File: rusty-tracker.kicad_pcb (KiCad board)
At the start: 4 copper layers, 50 x 85 mm, 172 parts, among them J1 SIM8051-6-0-14-01-X, J2 USB_C_Receptacle_USB2.0, J3 NFC, J4 tag-connect-swd, J5 Battery Connector, Q1 BC846, Q2 BC846, SW1 SW_Push, T1 Tab, T2 Tab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

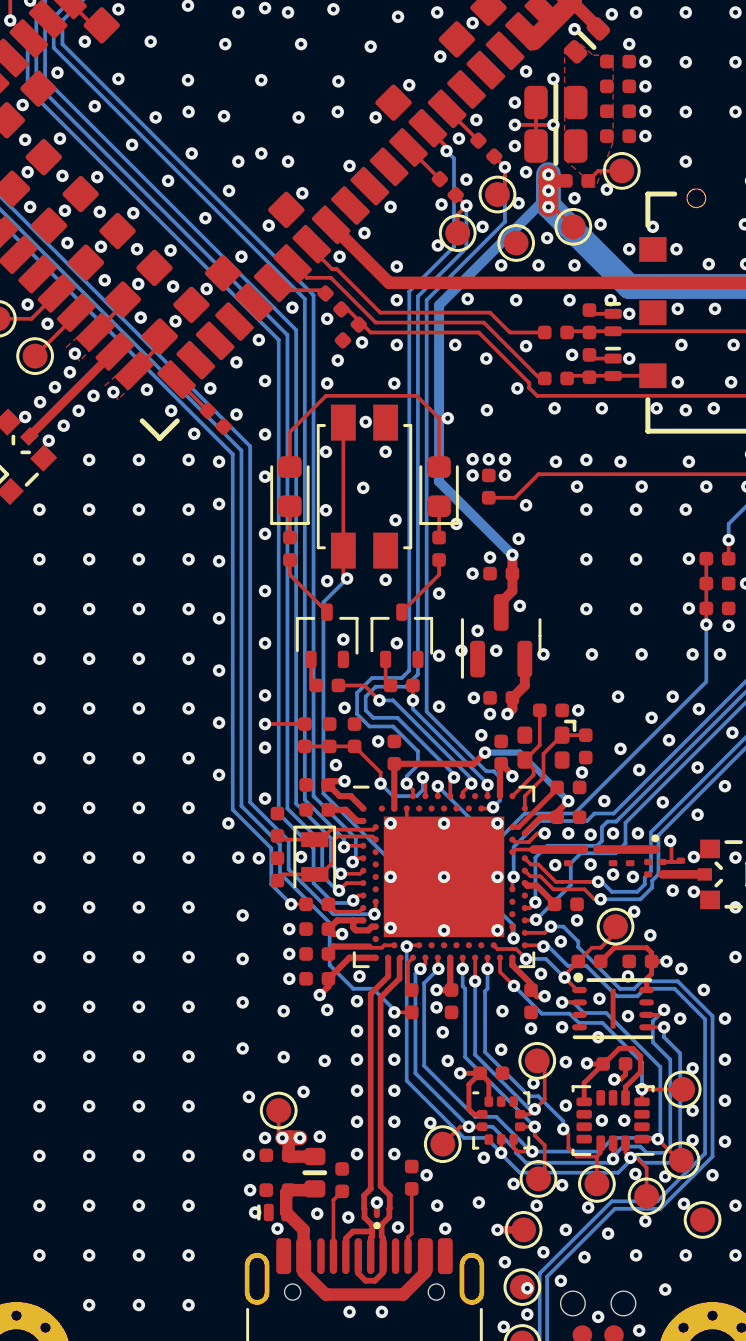
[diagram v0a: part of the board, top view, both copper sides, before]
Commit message: Add support for VBAT -> VDDH, and DCDC for the nRF52840
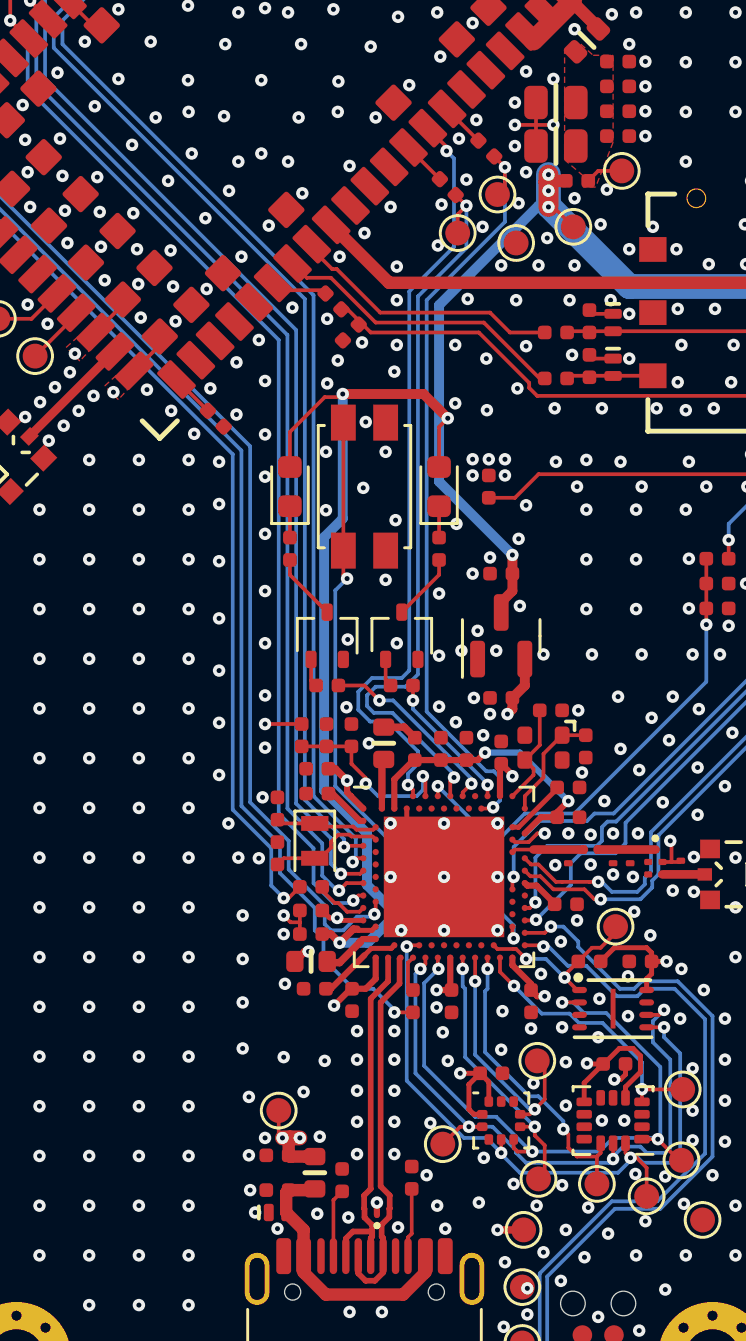
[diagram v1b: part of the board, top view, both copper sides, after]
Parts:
- added C41: 47n, passive:C_0402, F.Cu at (134.1, 135.6)
- added C45: 4.7u, passive:C_0402, F.Cu at (127.8, 143.0)
- added L10: 10u, passive:R_0603, F.Cu at (130.8, 135.3)
- added L4: 10u, passive:R_0603, F.Cu at (127.8, 144.1)
- added L9: 15n, passive:R_0402, F.Cu at (132.0, 135.6)
- moved C30 1.88 mm to (133.1, 135.6)
- moved C44 1.64 mm to (129.5, 145.7), turned to -90 degrees
- moved C43 1.40 mm to (128.0, 145.2)
- moved C28 0.79 mm to (127.8, 142.1)
- moved R25 0.74 mm to (127.8, 141.1)
- moved C10 0.65 mm to (128.1, 136.3)
- moved C11 0.65 mm to (126.5, 137.9)
- moved C13 0.65 mm to (126.5, 139.8)
- moved C39 0.65 mm to (128.1, 137.3)
- moved Y2 0.65 mm to (128.0, 139.2)
- moved C9 0.12 mm to (129.5, 135.0)
- moved R16 0.12 mm to (127.5, 135.0)
- moved R17 0.12 mm to (128.5, 135.0)
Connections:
- U2 pad AB2: unconnected-(U2-PadAB2) -> Net-(L4-Pad2)
- U2 pad B3: unconnected-(U2-PadB3) -> Net-(L10-Pad2)
- U2 pad Y2: +1V8 -> +BATT
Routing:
- net +BATT: track 78.5 -> 106.3 mm, vias 8 -> 10
- net Net-(L4-Pad2): track 0.00 -> 2.36 mm
- net Net-(L10-Pad2): track 0.00 -> 2.03 mm
- net GND: track 35.8 -> 37.5 mm, vias 998 -> 993
- net Net-(L10-Pad1): track 0.00 -> 1.43 mm
- net /LTE_RESET: track 43.8 -> 44.8 mm
- net +1V8: track 88.0 -> 89.0 mm, vias 11 -> 12
- net /BTN: track 26.2 -> 25.4 mm
- net VBUS: track 55.1 -> 55.9 mm
- net /DECUSB: track 2.79 -> 3.47 mm
- net /LTE_RTS: track 1.59 -> 2.21 mm
- net /VUSB_MEAS: track 7.24 -> 7.74 mm

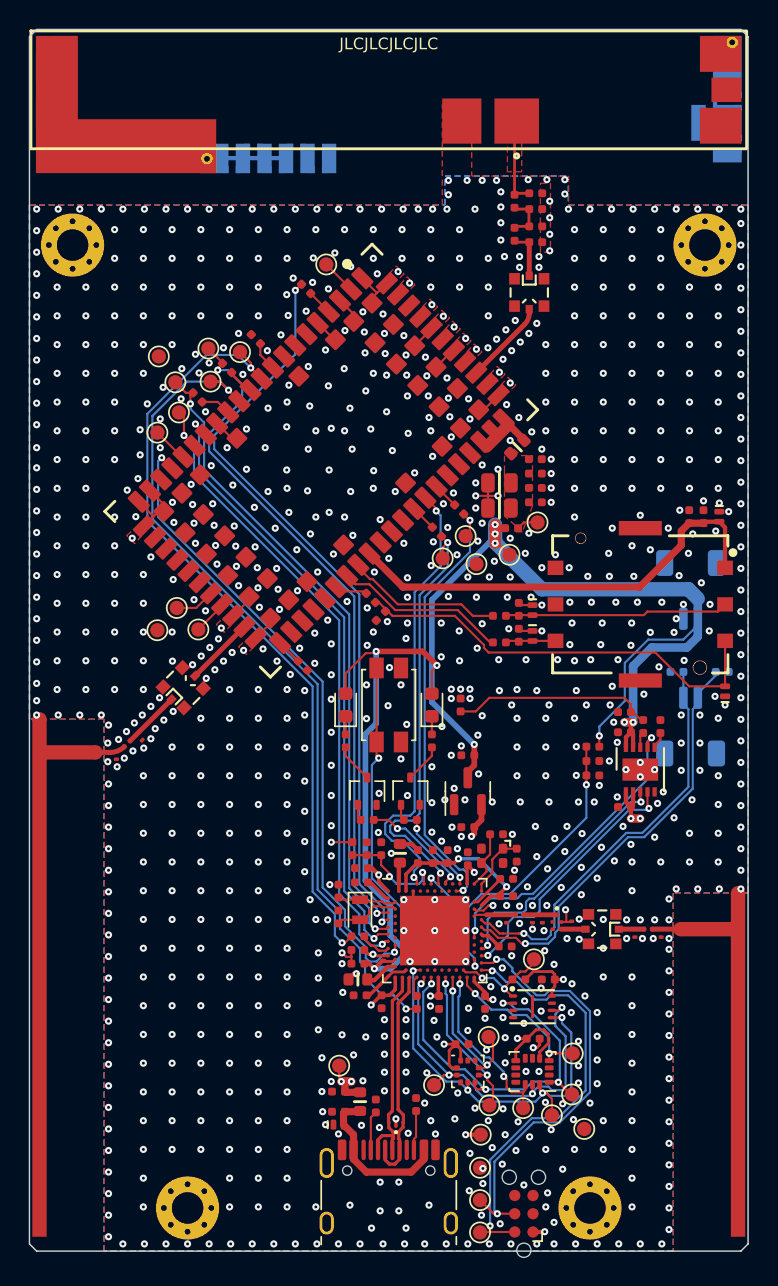
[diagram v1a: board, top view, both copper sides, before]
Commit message: Add protection & debounce to button
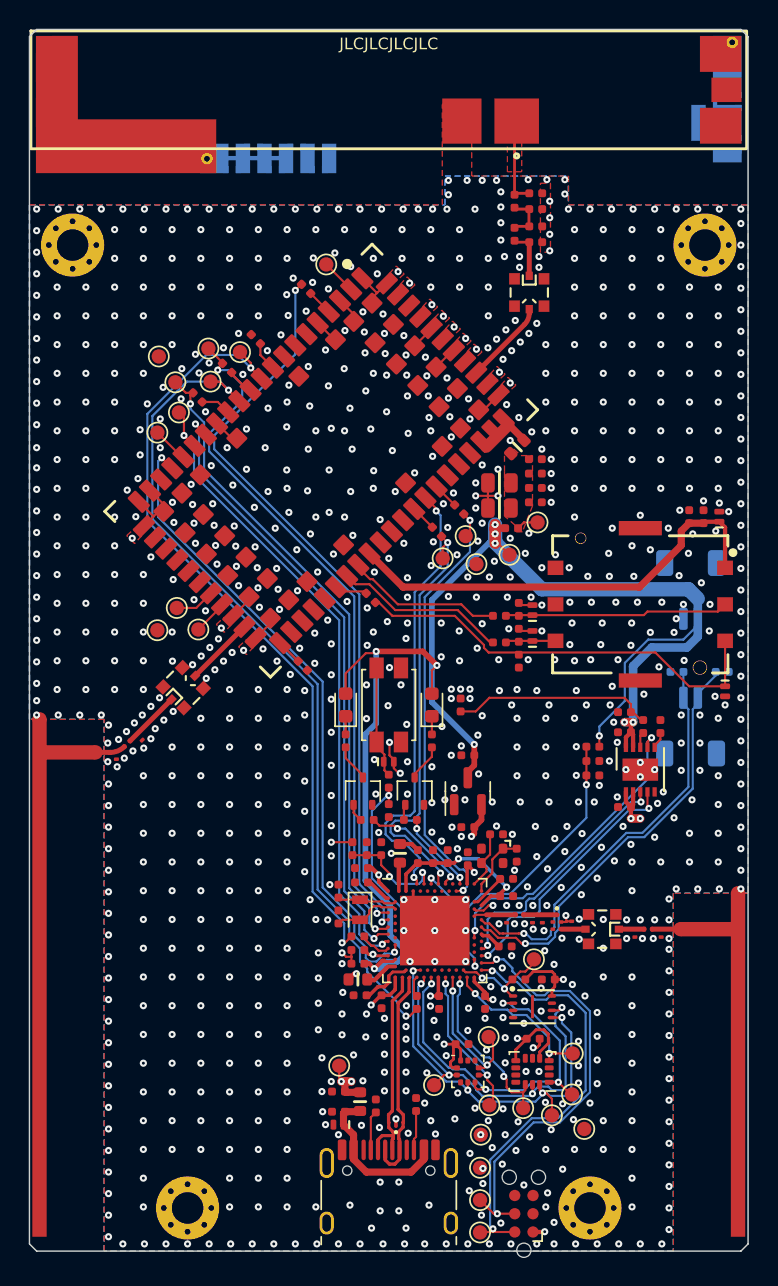
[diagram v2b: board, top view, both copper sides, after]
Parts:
- added C47: 0.1u, passive:C_0402, F.Cu at (130.0, 132.3)
- added D9: D_TVS, passive:D_0402_DFN1006, F.Cu at (130.0, 128.9)
- added R37: 100, passive:R_0402, F.Cu at (130.0, 130.3)
- moved C26 10.1 mm to (139.1, 122.0), turned to 90 degrees
- moved Q1 0.30 mm to (128.2, 131.0)
- moved Q2 0.30 mm to (131.8, 131.0)
- turned D3 to -90 degrees
- turned D4 to 90 degrees
- turned D5 to 90 degrees
- turned D6 to 90 degrees
- turned D7 to 180 degrees
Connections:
- D3 pad 1: GND -> /SIM_CLK_P
- D3 pad 2: /SIM_CLK_P -> GND
- D4 pad 1: GND -> /V_SIM_1V8
- D4 pad 2: /V_SIM_1V8 -> GND
- D5 pad 1: GND -> /SIM_IO_P
- D5 pad 2: /SIM_IO_P -> GND
- D6 pad 1: GND -> /SIM_RST_P
- D6 pad 2: /SIM_RST_P -> GND
- D7 pad 1: GND -> /VBUS_CON
- D7 pad 2: /VBUS_CON -> GND
- SW1 pad 1: /BTN -> Net-(D9-Pad1)
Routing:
- net Net-(D9-Pad1): track 0.00 -> 7.78 mm
- net /BTN: track 25.4 -> 18.0 mm
- net GND: track 37.5 -> 39.6 mm, vias 993 -> 1002
- net +1V8: track 89.0 -> 87.9 mm

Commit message: Make LDO DNP
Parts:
- U3: value MCP1700T-1802E/TT -> DNP
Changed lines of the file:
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@@
     (descr "SOT, 3 Pin (https://www.jedec.org/system/files/docs/to-236h.pdf variant AB), generated with kicad-footprint-generator ipc_gullwing_generator.py")
     (tags "SOT TO_SOT_SMD")
+    (property "MFPN" "MCP1700T-1802E/TT")
     (property "Sheetfile" "rusty-tracker.kicad_sch")
     (property "Sheetname" "")
@@
       (effects (font (size 1 1) (thickness 0.15)))
     )
-    (fp_text value "MCP1700T-1802E/TT" (at 0 2.4 90) (layer "F.Fab")
+    (fp_text value "DNP" (at 0 2.4 90) (layer "F.Fab")
       (effects (font (size 1 1) (thickness 0.15)))
     )

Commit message: Remove GND connection in screws
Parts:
- H1, H2, H3, H4: footprint MountingHole:MountingHole_2.2mm_M2_Pad_Via -> MountingHole:MountingHole_2.2mm_M2
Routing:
- net GND: vias 1002 -> 1041
